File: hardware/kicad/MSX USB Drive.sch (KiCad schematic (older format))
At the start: 9 parts, among them J1 Conn_02x25_Odd_Even, J2 Conn_02x08_Odd_Even, U1 74LS688, U2 74LS32

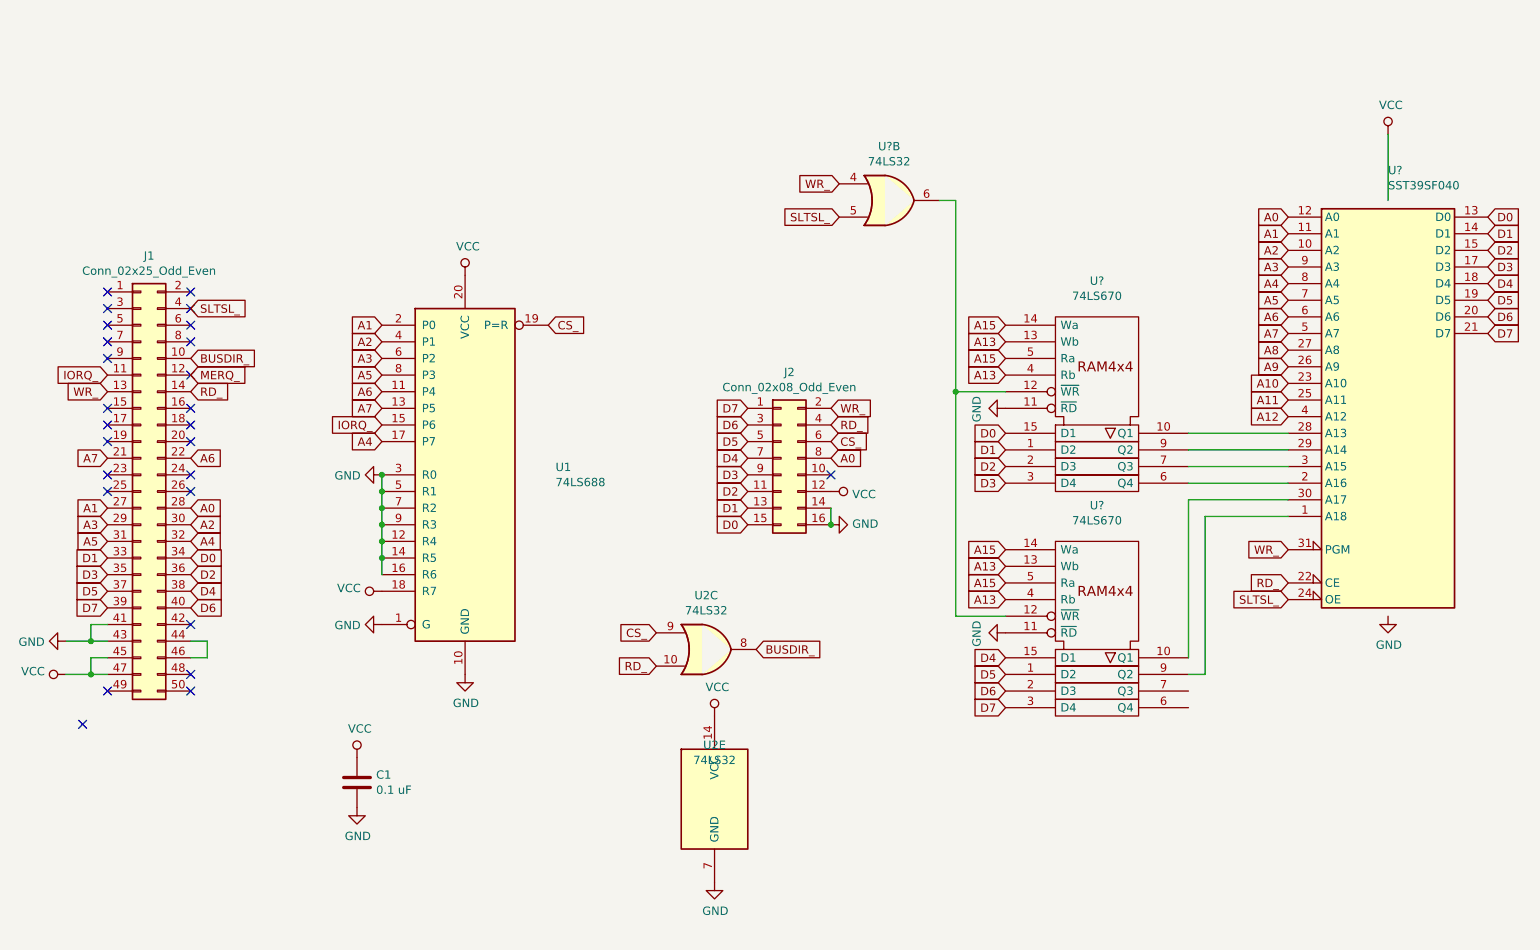
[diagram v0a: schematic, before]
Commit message: Added A13,A15 and updated IC numbering
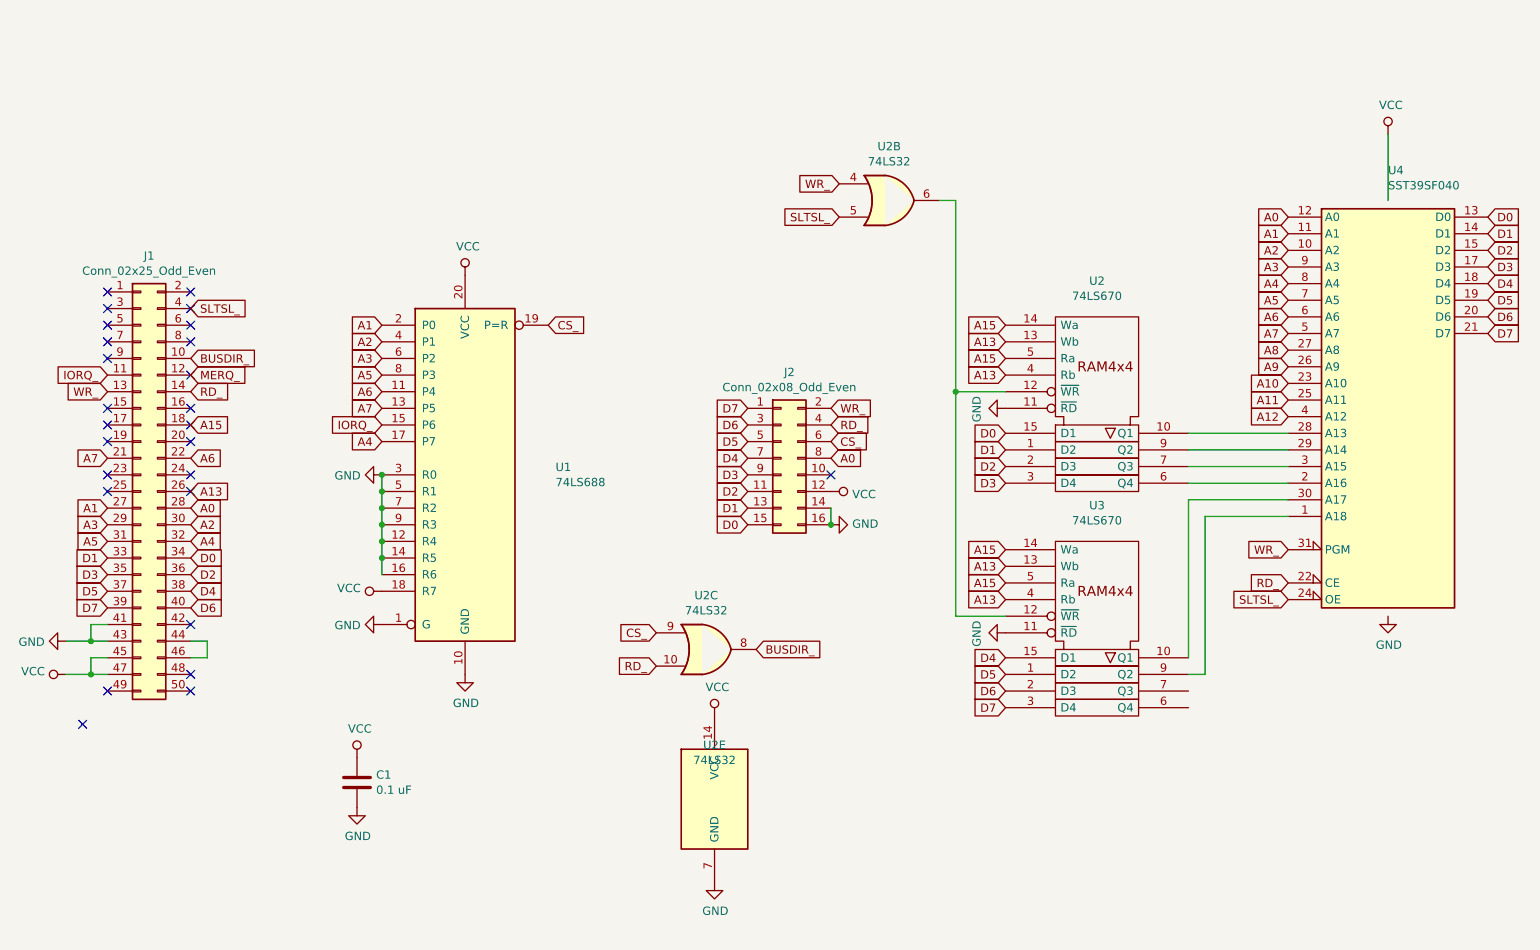
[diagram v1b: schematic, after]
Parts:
- gave numbers to parts that had none: 3
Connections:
- net A13: now also J1.26 (Pin_26)
- net A15: now also J1.18 (Pin_18)
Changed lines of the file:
@@
 $EndComp
 $Comp
-L power:VCC #PWR?
+L power:VCC #PWR0111
 U 1 1 5D5138BF
 P 5450 4950
-F 0 "#PWR?" H 5450 4800 50  0001 C CNN
+F 0 "#PWR0111" H 5450 4800 50  0001 C CNN
 F 1 "VCC" H 5467 5123 50  0000 C CNN
 F 2 "" H 5450 4950 50  0001 C CNN
@@
 $EndComp
 $Comp
-L power:GND #PWR?
+L power:GND #PWR0112
 U 1 1 5D514275
 P 5450 5950
-F 0 "#PWR?" H 5450 5700 50  0001 C CNN
+F 0 "#PWR0112" H 5450 5700 50  0001 C CNN
 F 1 "GND" H 5455 5777 50  0000 C CNN
 F 2 "" H 5450 5950 50  0001 C CNN
@@
 A12
 $Comp
-L 74xx_IEEE:74LS670 U?
+L 74xx_IEEE:74LS670 U2
 U 1 1 5DB8E9EF
 P 7750 3100
-F 0 "U?" H 7750 3866 50  0000 C CNN
+F 0 "U2" H 7750 3866 50  0000 C CNN
 F 1 "74LS670" H 7750 3775 50  0000 C CNN
 F 2 "" H 7750 3100 50  0001 C CNN
@@
 $EndComp
 $Comp
-L Memory_Flash:SST39SF040 U?
+L Memory_Flash:SST39SF040 U4
 U 1 1 5DB86845
 P 9500 3150
-F 0 "U?" H 9500 4631 50  0000 L CNN
+F 0 "U4" H 9500 4631 50  0000 L CNN
 F 1 "SST39SF040" H 9500 4540 50  0000 L CNN
 F 2 "" H 9500 3450 50  0001 C CNN
@@
 $EndComp
 $Comp
-L 74xx_IEEE:74LS670 U?
+L 74xx_IEEE:74LS670 U3
 U 1 1 5DB9E92E
 P 7750 4450
-F 0 "U?" H 7750 5216 50  0000 C CNN
+F 0 "U3" H 7750 5216 50  0000 C CNN
 F 1 "74LS670" H 7750 5125 50  0000 C CNN
 F 2 "" H 7750 4450 50  0001 C CNN
@@
 	8400 3750 8900 3750
 $Comp
-L power:GND #PWR?
+L power:GND #PWR0113
 U 1 1 5DBA29A0
 P 9500 4350
-F 0 "#PWR?" H 9500 4100 50  0001 C CNN
+F 0 "#PWR0113" H 9500 4100 50  0001 C CNN
 F 1 "GND" H 9505 4177 50  0000 C CNN
 F 2 "" H 9500 4350 50  0001 C CNN
@@
 $EndComp
 $Comp
-L power:VCC #PWR?
+L power:VCC #PWR0114
 U 1 1 5DBA455B
 P 9500 1450
-F 0 "#PWR?" H 9500 1300 50  0001 C CNN
+F 0 "#PWR0114" H 9500 1300 50  0001 C CNN
 F 1 "VCC" H 9517 1623 50  0000 C CNN
 F 2 "" H 9500 1450 50  0001 C CNN
@@
 D7
 $Comp
-L power:GND #PWR?
+L power:GND #PWR0115
 U 1 1 5DBB7136
 P 7200 3100
-F 0 "#PWR?" H 7200 2850 50  0001 C CNN
+F 0 "#PWR0115" H 7200 2850 50  0001 C CNN
 F 1 "GND" H 7205 2927 50  0000 C CNN
 F 2 "" H 7200 3100 50  0001 C CNN
@@
 $EndComp
 $Comp
-L power:GND #PWR?
+L power:GND #PWR0116
 U 1 1 5DBB82A9
 P 7200 4450
-F 0 "#PWR?" H 7200 4200 50  0001 C CNN
+F 0 "#PWR0116" H 7200 4200 50  0001 C CNN
 F 1 "GND" H 7205 4277 50  0000 C CNN
 F 2 "" H 7200 4450 50  0001 C CNN
@@
 $EndComp
 $Comp
-L 74xx:74LS32 U?
+L 74xx:74LS32 U2
 U 2 1 5DBB94CC
 P 6500 1850
-F 0 "U?" H 6500 2175 50  0000 C CNN
+F 0 "U2" H 6500 2175 50  0000 C CNN
 F 1 "74LS32" H 6500 2084 50  0000 C CNN
 F 2 "" H 6500 1850 50  0001 C CNN
@@
 Text GLabel 8900 3950 0    50   Input ~ 0
 WR_
+Text GLabel 2300 3200 2    50   Input ~ 0
+A15
+Text GLabel 2300 3600 2    50   Input ~ 0
+A13
 $EndSCHEMATC

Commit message: PCB first attempt
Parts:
- added C2, C3, C4, C5: 0.1 uF, Capacitor_THT:C_Radial_D6.3mm_H5.0mm_P2.50mm, symbol Device:C
- added unit 3 of U1
- added unit 1 of U1
- C1: footprint (none) -> Capacitor_THT:C_Radial_D6.3mm_H5.0mm_P2.50mm
- J1: footprint (none) -> MSX cartridge:msx_cartridge
- J2: footprint (none) -> Connector_PinHeader_2.54mm:PinHeader_2x08_P2.54mm_Vertical
- U1: renamed from U2; footprint (none) -> Package_DIP:DIP-14_W7.62mm_Socket
- U2: renamed from U1; footprint (none) -> Package_DIP:DIP-20_W7.62mm_Socket
- U3: renamed from U2; footprint (none) -> Package_DIP:DIP-16_W7.62mm_Socket
- U4: renamed from U3; footprint (none) -> Package_DIP:DIP-16_W7.62mm_Socket
- U5: renamed from U4; footprint (none) -> Package_DIP:DIP-32_W15.24mm_Socket
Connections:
- net A10: now also J1.20 (Pin_20)
- net A11: now also J1.19 (Pin_19)
- net A12: now also J1.23 (Pin_23)
- net A8: now also J1.24 (Pin_24)
- net A9: now also J1.17 (Pin_17)
- net BUSDIR_: now also U1.6; no longer U1.8
- net CS_: now also U1.4; no longer U1.9
- net GND: now also C2.2, C3.2, C4.2, C5.2, U1.1, U1.10, U1.2, U1.9
- net RD_: now also U1.5; no longer U1.10
- net SLTSL_: now also U1.13; no longer U1.5
- net VCC: now also C2.1, C3.1, C4.1, C5.1
- net WR_: now also U1.12; no longer U1.4
- net at U3.12 (~WR), U4.12 (~WR): now also U1.11; no longer U1.6
- net MERQ_: no longer names the net of J1.12 (Pin_12)
- no-connect marks 26 -> 21
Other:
- moved on the sheet: C1, U1E
